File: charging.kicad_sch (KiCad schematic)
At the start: 11 parts, among them SW1 SW_SPDT, U2 BQ24075RGT

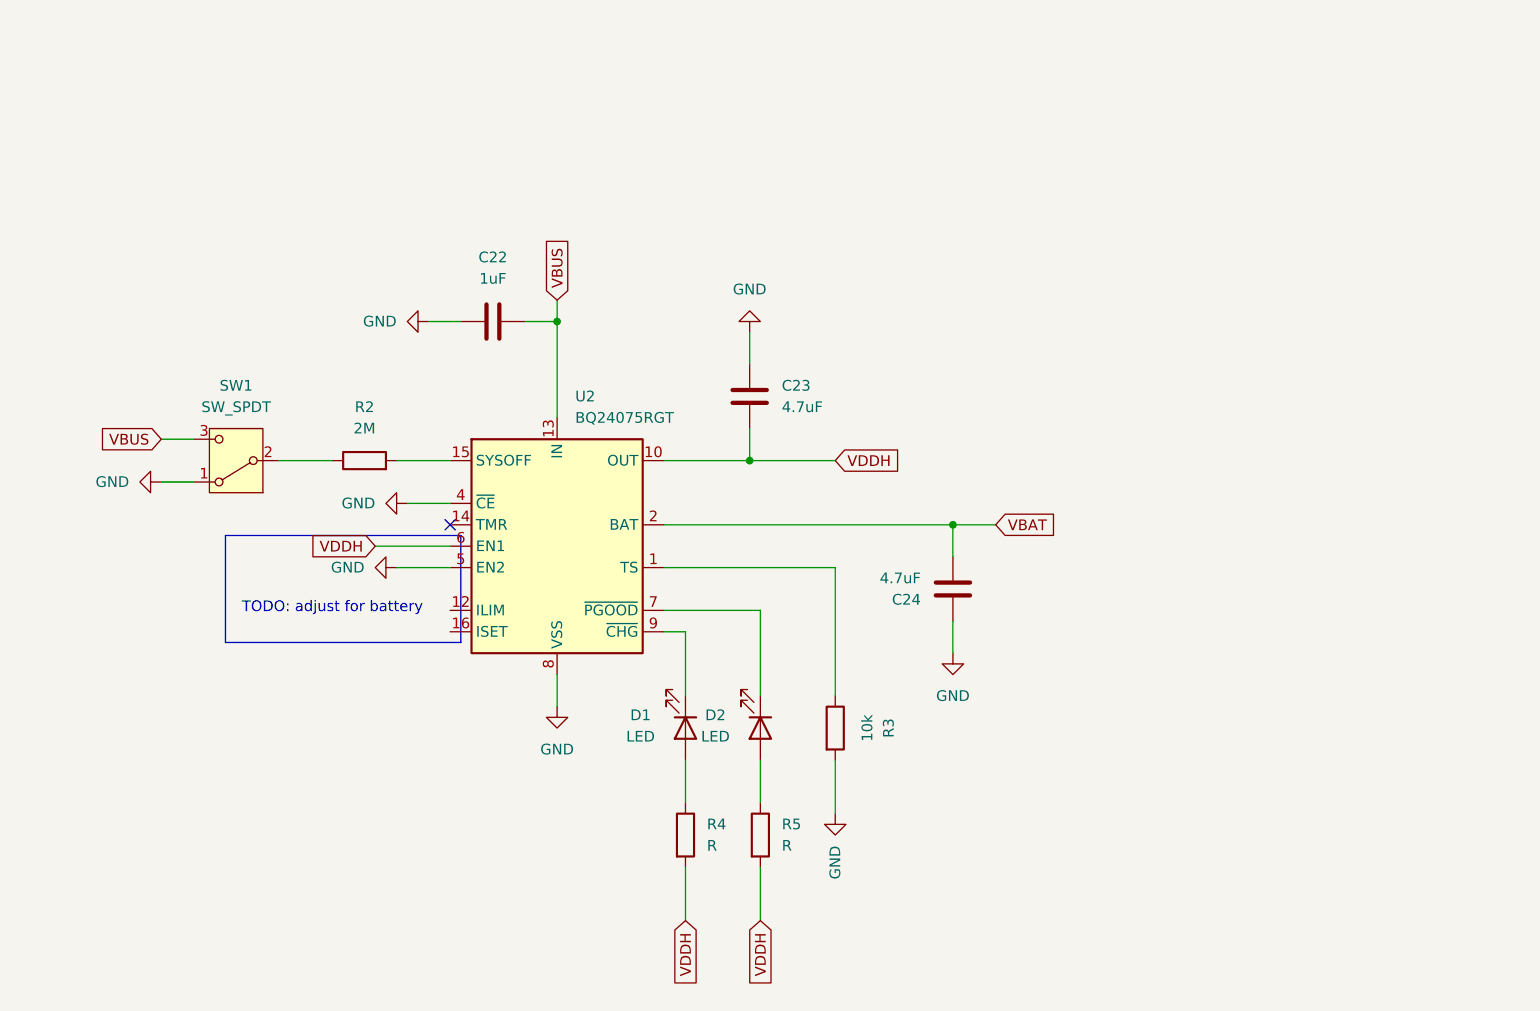
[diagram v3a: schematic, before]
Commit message: Added ISET and JST to Battery
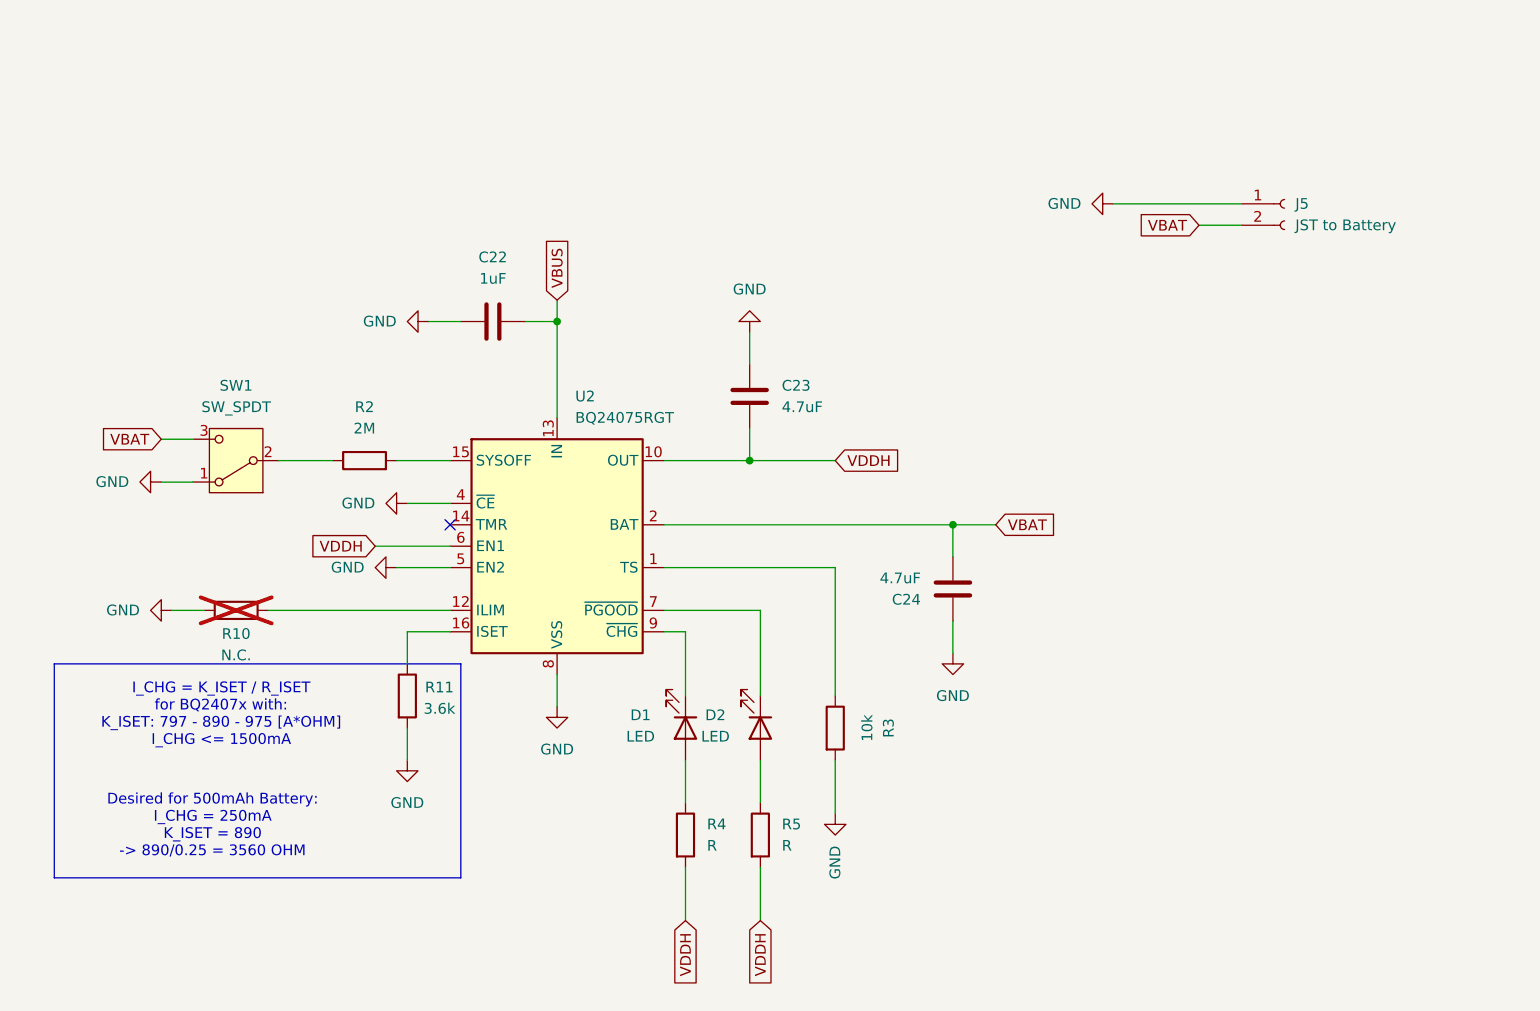
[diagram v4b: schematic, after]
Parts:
- added J5: JST to Battery, Connector_JST:JST_PH_S2B-PH-K_1x02_P2.00mm_Horizontal, symbol Connector:Conn_01x02_Socket
- added R10: N.C., symbol Device:R
- added R11: 3.6k, symbol Device:R
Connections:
- net GND: now also J5.1 (Pin_1), R10.2, R11.2
- net VBAT: now also SW1.3 (C), J5.2 (Pin_2)
- net VBUS: no longer SW1.3 (C)
- net at U2.12 (ILIM): now also R10.1
- net at U2.16 (ISET): now also R11.1
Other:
- note added: "Desired for 500mAh Battery: I_CHG = 250mA K_ISET = 890 -> 890/0.25 = 3560 OHM"
- note added: "I_CHG = K_ISET / R_ISET for BQ2407x with: K_ISET: 797 - 890 - 975 [A*OHM] I_CHG <= 1500mA"
- note removed: "TODO: adjust for battery"

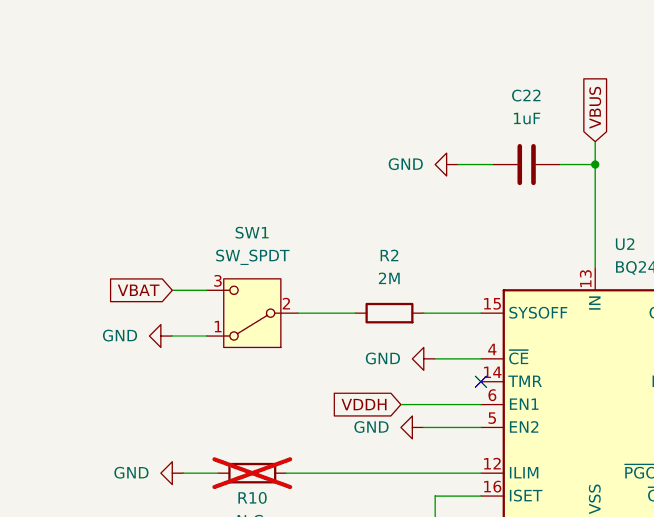
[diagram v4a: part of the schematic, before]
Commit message: Updated Footprints
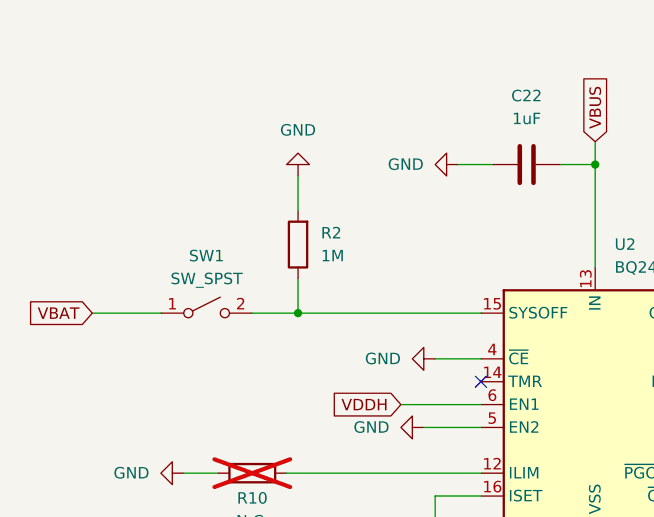
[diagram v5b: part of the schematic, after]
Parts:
- removed SW1: SW_SPDT, symbol Switch:SW_SPDT
- added SW1: SW_SPST, symbol Switch:SW_SPST
- C22, C23: footprint (none) -> Capacitor_SMD:C_0402_1005Metric
- C24: footprint (none) -> Capacitor_SMD:C_0603_1608Metric
- R10, R11, R3, R4, R5: footprint (none) -> Resistor_SMD:R_0603_1608Metric
- R2: value 2M -> 1M; footprint (none) -> Resistor_SMD:R_0603_1608Metric
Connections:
- net GND: now also R2.2
- net VBAT: now also SW1.1 (A)
- net at R2.1: now also U2.15 (SYSOFF), SW1.2 (B)
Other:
- moved on the sheet: R2
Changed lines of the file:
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@@
+	)
+	(junction
+		(at 109.22 77.47)
+		(diameter 0)
+		(color 0 0 0 0)
 	)
 	(junction
@@
 	(wire
 		(pts
+			(xy 109.22 73.66) (xy 109.22 77.47)
+		)
+		(stroke
+			(width 0)
+			(type default)
+		)
+	)
+	(wire
+		(pts
 			(xy 96.52 95.25) (xy 100.33 95.25)
 		)
@@
 	(wire
 		(pts
+			(xy 109.22 77.47) (xy 129.54 77.47)
+		)
+		(stroke
+			(width 0)
+			(type default)
+		)
+	)
+	(wire
+		(pts
 			(xy 127 60.96) (xy 130.81 60.96)
 		)
@@
 	(wire
 		(pts
-			(xy 109.22 77.47) (xy 115.57 77.47)
+			(xy 104.14 77.47) (xy 109.22 77.47)
 		)
 		(stroke
@@
 	(wire
 		(pts
-			(xy 95.25 74.93) (xy 99.06 74.93)
+			(xy 109.22 62.23) (xy 109.22 66.04)
+		)
+		(stroke
+			(width 0)
+			(type default)
+		)
+	)
+	(wire
+		(pts
+			(xy 86.36 77.47) (xy 93.98 77.47)
 		)
 		(stroke
@@
 	(wire
 		(pts
-			(xy 123.19 77.47) (xy 129.54 77.47)
-		)
-		(stroke
-			(width 0)
-			(type default)
-		)
-	)
-	(wire
-		(pts
 			(xy 107.95 95.25) (xy 129.54 95.25)
 		)
@@
 		(pts
 			(xy 124.46 82.55) (xy 129.54 82.55)
-		)
-		(stroke
-			(width 0)
-			(type default)
-		)
-	)
-	(wire
-		(pts
-			(xy 95.25 80.01) (xy 99.06 80.01)
 		)
 		(stroke
@@
 	(global_label "VBAT"
 		(shape input)
-		(at 95.25 74.93 180)
+		(at 86.36 77.47 180)
 		(fields_autoplaced yes)
 		(effects
@@
 		)
 		(property "Intersheetrefs" "${INTERSHEET_REFS}"
-			(at 87.85 74.93 0)
+			(at 78.96 77.47 0)
 			(effects
 				(font
@@
 			)
 		)
-		(property "Footprint" ""
+		(property "Footprint" "Capacitor_SMD:C_0603_1608Metric"
 			(at 190.1952 96.52 0)
 			(effects
@@
 			)
 		)
-		(property "Footprint" ""
+		(property "Footprint" "Resistor_SMD:R_0603_1608Metric"
 			(at 122.682 105.41 90)
 			(effects
@@
 			)
 		)
-		(property "Footprint" ""
+		(property "Footprint" "Capacitor_SMD:C_0402_1005Metric"
 			(at 138.43 59.9948 0)
 			(effects
@@
 			)
 		)
-		(property "Footprint" ""
+		(property "Footprint" "Capacitor_SMD:C_0402_1005Metric"
 			(at 164.1348 66.04 0)
 			(effects
@@
 			)
 		)
-		(property "Footprint" ""
+		(property "Footprint" "Resistor_SMD:R_0603_1608Metric"
 			(at 173.482 109.22 90)
 			(effects
@@
 	(symbol
 		(lib_id "Device:R")
-		(at 119.38 77.47 90)
+		(at 109.22 69.85 180)
 		(unit 1)
 		(exclude_from_sim no)
@@
 		(fields_autoplaced yes)
 		(property "Reference" "R2"
-			(at 119.38 71.12 90)
-			(effects
-				(font
-					(size 1.27 1.27)
-				)
-			)
-		)
-		(property "Value" "2M"
-			(at 119.38 73.66 90)
-			(effects
-				(font
-					(size 1.27 1.27)
-				)
-			)
-		)
-		(property "Footprint" ""
-			(at 119.38 79.248 90)
+			(at 111.76 68.5799 0)
+			(effects
+				(font
+					(size 1.27 1.27)
+				)
+				(justify right)
+			)
+		)
+		(property "Value" "1M"
+			(at 111.76 71.1199 0)
+			(effects
+				(font
+					(size 1.27 1.27)
+				)
+				(justify right)
+			)
+		)
+		(property "Footprint" "Resistor_SMD:R_0603_1608Metric"
+			(at 110.998 69.85 90)
 			(effects
 				(font
@@
 		)
 		(property "Datasheet" "~"
-			(at 119.38 77.47 0)
+			(at 109.22 69.85 0)
 			(effects
 				(font
@@
 		)
 		(property "Description" "Resistor"
-			(at 119.38 77.47 0)
+			(at 109.22 69.85 0)
 			(effects
 				(font
@@
 	)
 	(symbol
-		(lib_id "Switch:SW_SPDT")
-		(at 104.14 77.47 180)
+		(lib_id "power:GND")
+		(at 109.22 62.23 180)
 		(unit 1)
 		(exclude_from_sim no)
@@
 		(dnp no)
 		(fields_autoplaced yes)
-		(property "Reference" "SW1"
-			(at 104.14 68.58 0)
-			(effects
-				(font
-					(size 1.27 1.27)
-				)
-			)
-		)
-		(property "Value" "SW_SPDT"
-			(at 104.14 71.12 0)
+		(property "Reference" "#PWR019"
+			(at 109.22 55.88 0)
+			(effects
+				(font
+					(size 1.27 1.27)
+				)
+				(hide yes)
+			)
+		)
+		(property "Value" "GND"
+			(at 109.22 57.15 0)
 			(effects
 				(font
@@
 		)
 		(property "Footprint" ""
-			(at 104.14 77.47 0)
-			(effects
-				(font
-					(size 1.27 1.27)
-				)
-				(hide yes)
-			)
-		)
-		(property "Datasheet" "~"
-			(at 104.14 69.85 0)
-			(effects
-				(font
-					(size 1.27 1.27)
-				)
-				(hide yes)
-			)
-		)
-		(property "Description" "Switch, single pole double throw"
-			(at 104.14 77.47 0)
-			(effects
-				(font
-					(size 1.27 1.27)
-				)
-				(hide yes)
-			)
-		)
-		(pin "1"
-		)
-		(pin "2"
-		)
-		(pin "3"
-		)
-		(instances
-			(project ""
-				(path "/5d65a0d4-45a3-4af0-996a-c0381d04499a/f42a8a8a-4a34-440a-8e58-9c442fe0d23e/8d78fcfc-e335-4768-b7c7-c99d7af02414"
-					(reference "SW1")
-					(unit 1)
-				)
-			)
-		)
-	)
-	(symbol
-		(lib_id "power:GND")
-		(at 95.25 80.01 270)
-		(unit 1)
-		(exclude_from_sim no)
-		(in_bom yes)
-		(on_board yes)
-		(dnp no)
-		(fields_autoplaced yes)
-		(property "Reference" "#PWR019"
-			(at 88.9 80.01 0)
-			(effects
-				(font
-					(size 1.27 1.27)
-				)
-				(hide yes)
-			)
-		)
-		(property "Value" "GND"
-			(at 91.44 80.0099 90)
-			(effects
-				(font
-					(size 1.27 1.27)
-				)
-				(justify right)
-			)
-		)
-		(property "Footprint" ""
-			(at 95.25 80.01 0)
+			(at 109.22 62.23 0)
 			(effects
 				(font
@@
 		)
 		(property "Datasheet" ""
-			(at 95.25 80.01 0)
+			(at 109.22 62.23 0)
 			(effects
 				(font
@@
 		)
 		(property "Description" "Power symbol creates a global label with name \"GND\" , ground"
-			(at 95.25 80.01 0)
+			(at 109.22 62.23 0)
 			(effects
 				(font
@@
 			)
 		)
-		(property "Footprint" ""
+		(property "Footprint" "Resistor_SMD:R_0603_1608Metric"
 			(at 104.14 93.472 90)
 			(effects
@@
 	)
 	(symbol
+		(lib_id "Switch:SW_SPST")
+		(at 99.06 77.47 0)
+		(unit 1)
+		(exclude_from_sim no)
+		(in_bom yes)
+		(on_board yes)
+		(dnp no)
+		(fields_autoplaced yes)
+		(property "Reference" "SW1"
+			(at 99.06 71.12 0)
+			(effects
+				(font
+					(size 1.27 1.27)
+				)
+			)
+		)
+		(property "Value" "SW_SPST"
+			(at 99.06 73.66 0)
+			(effects
+				(font
+					(size 1.27 1.27)
+				)
+			)
+		)
+		(property "Footprint" ""
+			(at 99.06 77.47 0)
+			(effects
+				(font
+					(size 1.27 1.27)
+				)
+				(hide yes)
+			)
+		)
+		(property "Datasheet" "~"
+			(at 99.06 77.47 0)
+			(effects
+				(font
+					(size 1.27 1.27)
+				)
+				(hide yes)
+			)
+		)
+		(property "Description" "Single Pole Single Throw (SPST) switch"
+			(at 99.06 77.47 0)
+			(effects
+				(font
+					(size 1.27 1.27)
+				)
+				(hide yes)
+			)
+		)
+		(pin "1"
+		)
+		(pin "2"
+		)
+		(instances
+			(project ""
+				(path "/5d65a0d4-45a3-4af0-996a-c0381d04499a/f42a8a8a-4a34-440a-8e58-9c442fe0d23e/8d78fcfc-e335-4768-b7c7-c99d7af02414"
+					(reference "SW1")
+					(unit 1)
+				)
+			)
+		)
+	)
+	(symbol
 		(lib_id "Battery_Management:BQ24075RGT")
 		(at 142.24 87.63 0)
@@
 			)
 		)
-		(property "Footprint" ""
+		(property "Footprint" "Resistor_SMD:R_0603_1608Metric"
 			(at 164.592 121.92 90)
 			(effects
@@
 			)
 		)
-		(property "Footprint" ""
+		(property "Footprint" "Resistor_SMD:R_0603_1608Metric"
 			(at 155.702 121.92 90)
 			(effects

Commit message: Updated Footprints
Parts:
- removed SW1: SW_SPST, symbol Switch:SW_SPST
- added BT1: Li-Ion, 500mAh, 3,7V, symbol Device:Battery
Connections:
- net SYSOFF_SWITCH: now reaches R2.1, U2.15 (SYSOFF)
- no-connect marks 1 -> 3
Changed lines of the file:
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@@
 		(at 129.54 85.09)
 	)
+	(no_connect
+		(at 227.33 35.56)
+	)
+	(no_connect
+		(at 227.33 25.4)
+	)
 	(wire
 		(pts
@@
 	(wire
 		(pts
+			(xy 102.87 77.47) (xy 109.22 77.47)
+		)
+		(stroke
+			(width 0)
+			(type default)
+		)
+	)
+	(wire
+		(pts
 			(xy 165.1 77.47) (xy 175.26 77.47)
 		)
@@
 	(wire
 		(pts
-			(xy 104.14 77.47) (xy 109.22 77.47)
-		)
-		(stroke
-			(width 0)
-			(type default)
-		)
-	)
-	(wire
-		(pts
 			(xy 154.94 85.09) (xy 189.23 85.09)
 		)
@@
 		(pts
 			(xy 109.22 62.23) (xy 109.22 66.04)
-		)
-		(stroke
-			(width 0)
-			(type default)
-		)
-	)
-	(wire
-		(pts
-			(xy 86.36 77.47) (xy 93.98 77.47)
 		)
 		(stroke
@@
 		)
 	)
-	(global_label "VBAT"
+	(global_label "VDDH"
 		(shape input)
-		(at 86.36 77.47 180)
+		(at 120.65 87.63 180)
 		(fields_autoplaced yes)
 		(effects
@@
 		)
 		(property "Intersheetrefs" "${INTERSHEET_REFS}"
-			(at 78.96 77.47 0)
+			(at 112.7057 87.63 0)
 			(effects
 				(font
@@
 	(global_label "VDDH"
 		(shape input)
-		(at 120.65 87.63 180)
+		(at 157.48 132.08 270)
 		(fields_autoplaced yes)
 		(effects
@@
 		)
 		(property "Intersheetrefs" "${INTERSHEET_REFS}"
-			(at 112.7057 87.63 0)
+			(at 157.48 140.0243 90)
 			(effects
 				(font
@@
 	(global_label "VDDH"
 		(shape input)
-		(at 157.48 132.08 270)
+		(at 166.37 132.08 270)
 		(fields_autoplaced yes)
 		(effects
@@
 		)
 		(property "Intersheetrefs" "${INTERSHEET_REFS}"
-			(at 157.48 140.0243 90)
+			(at 166.37 140.0243 90)
 			(effects
 				(font
@@
 		)
 	)
-	(global_label "VDDH"
+	(global_label "SYSOFF_SWITCH"
 		(shape input)
-		(at 166.37 132.08 270)
+		(at 102.87 77.47 180)
 		(fields_autoplaced yes)
 		(effects
@@
 		)
 		(property "Intersheetrefs" "${INTERSHEET_REFS}"
-			(at 166.37 140.0243 90)
+			(at 85.0681 77.47 0)
 			(effects
 				(font
@@
 				(path "/5d65a0d4-45a3-4af0-996a-c0381d04499a/f42a8a8a-4a34-440a-8e58-9c442fe0d23e/8d78fcfc-e335-4768-b7c7-c99d7af02414"
 					(reference "C24")
+					(unit 1)
+				)
+			)
+		)
+	)
+	(symbol
+		(lib_id "Device:Battery")
+		(at 227.33 30.48 0)
+		(unit 1)
+		(exclude_from_sim no)
+		(in_bom yes)
+		(on_board no)
+		(dnp no)
+		(fields_autoplaced yes)
+		(property "Reference" "BT1"
+			(at 231.14 28.6384 0)
+			(effects
+				(font
+					(size 1.27 1.27)
+				)
+				(justify left)
+			)
+		)
+		(property "Value" "Li-Ion, 500mAh, 3,7V"
+			(at 231.14 31.1784 0)
+			(effects
+				(font
+					(size 1.27 1.27)
+				)
+				(justify left)
+			)
+		)
+		(property "Footprint" ""
+			(at 227.33 28.956 90)
+			(effects
+				(font
+					(size 1.27 1.27)
+				)
+				(hide yes)
+			)
+		)
+		(property "Datasheet" "~"
+			(at 227.33 28.956 90)
+			(effects
+				(font
+					(size 1.27 1.27)
+				)
+				(hide yes)
+			)
+		)
+		(property "Description" "https://www.reichelt.de/de/de/shop/produkt/li-ion_akku_soldered_333278_500_mah_3_7_v-373542?PROVID=2788&gad_source=1&gad_campaignid=1622074784&gclid=CjwKCAiAzOXMBhASEiwAe14SaXFzLofdcSumYexdSOb9ls3UI7x2JoZZgAI9023aiDUEpTiuzRkwshoC6d0QAvD_BwE#closemodal"
+			(at 227.33 30.48 0)
+			(effects
+				(font
+					(size 1.27 1.27)
+				)
+				(hide yes)
+			)
+		)
+		(pin "2"
+		)
+		(pin "1"
+		)
+		(instances
+			(project ""
+				(path "/5d65a0d4-45a3-4af0-996a-c0381d04499a/f42a8a8a-4a34-440a-8e58-9c442fe0d23e/8d78fcfc-e335-4768-b7c7-c99d7af02414"
+					(reference "BT1")
 					(unit 1)
 				)
@@
 					(unit 1)
 				)
-			)
-		)
-	)
-	(symbol
-		(lib_id "Switch:SW_SPST")
-		(at 99.06 77.47 0)
-		(unit 1)
-		(exclude_from_sim no)
-		(in_bom yes)
-		(on_board yes)
-		(dnp no)
-		(fields_autoplaced yes)
-		(property "Reference" "SW1"
-			(at 99.06 71.12 0)
-			(effects
-				(font
-					(size 1.27 1.27)
-				)
-			)
-		)
-		(property "Value" "SW_SPST"
-			(at 99.06 73.66 0)
-			(effects
-				(font
-					(size 1.27 1.27)
-				)
-			)
-		)
-		(property "Footprint" ""
-			(at 99.06 77.47 0)
-			(effects
-				(font
-					(size 1.27 1.27)
-				)
-				(hide yes)
-			)
-		)
-		(property "Datasheet" "~"
-			(at 99.06 77.47 0)
-			(effects
-				(font
-					(size 1.27 1.27)
-				)
-				(hide yes)
-			)
-		)
-		(property "Description" "Single Pole Single Throw (SPST) switch"
-			(at 99.06 77.47 0)
-			(effects
-				(font
-					(size 1.27 1.27)
-				)
-				(hide yes)
-			)
-		)
-		(pin "1"
-		)
-		(pin "2"
-		)
-		(instances
-			(project ""
-				(path "/5d65a0d4-45a3-4af0-996a-c0381d04499a/f42a8a8a-4a34-440a-8e58-9c442fe0d23e/8d78fcfc-e335-4768-b7c7-c99d7af02414"
-					(reference "SW1")
-					(unit 1)
-				)
